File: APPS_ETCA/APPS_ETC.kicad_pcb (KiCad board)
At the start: 2 copper layers, 93.5 x 69.6 mm, 27 parts, among them P1 DTM1312PC12PDR008, U1 NUCLEO-L432KC, U2 MCP6004, U6 LM7805_TO220, U8 LM7809_TO220

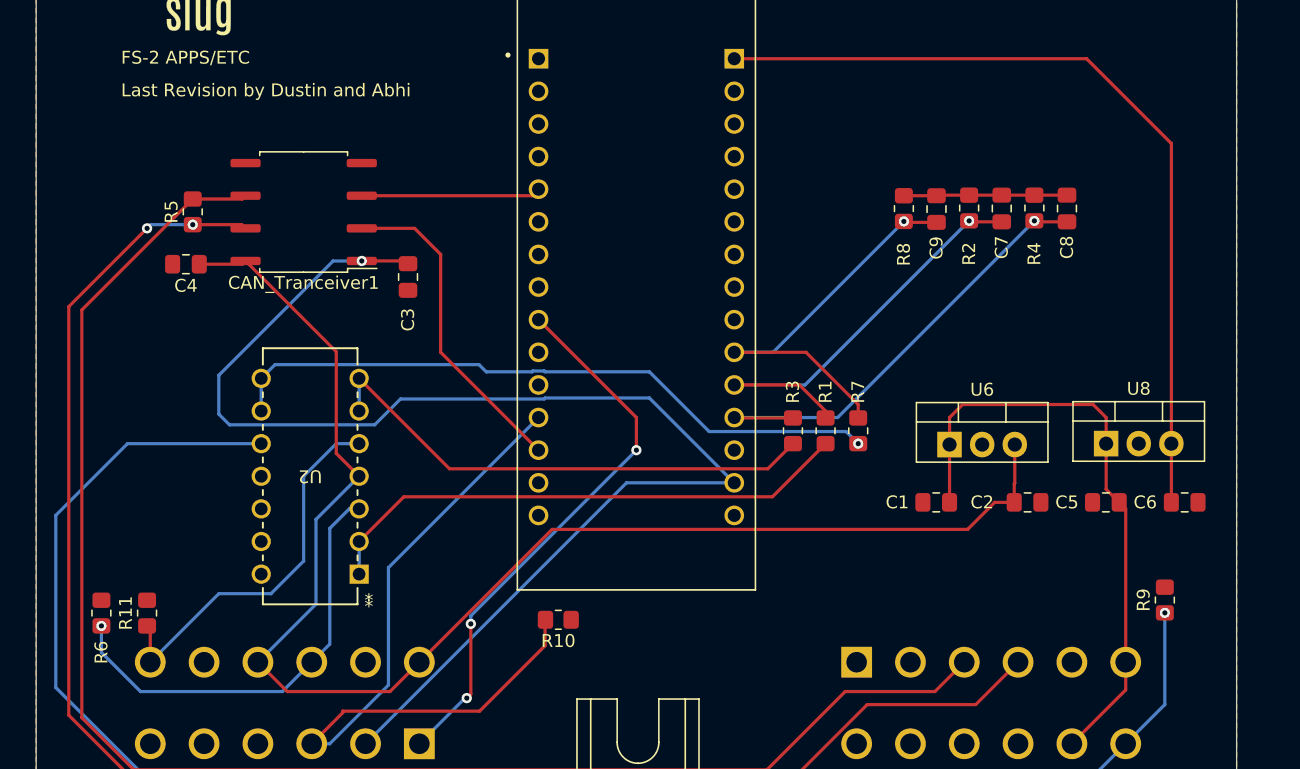
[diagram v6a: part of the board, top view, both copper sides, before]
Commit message: silk screen update again (please dont break)
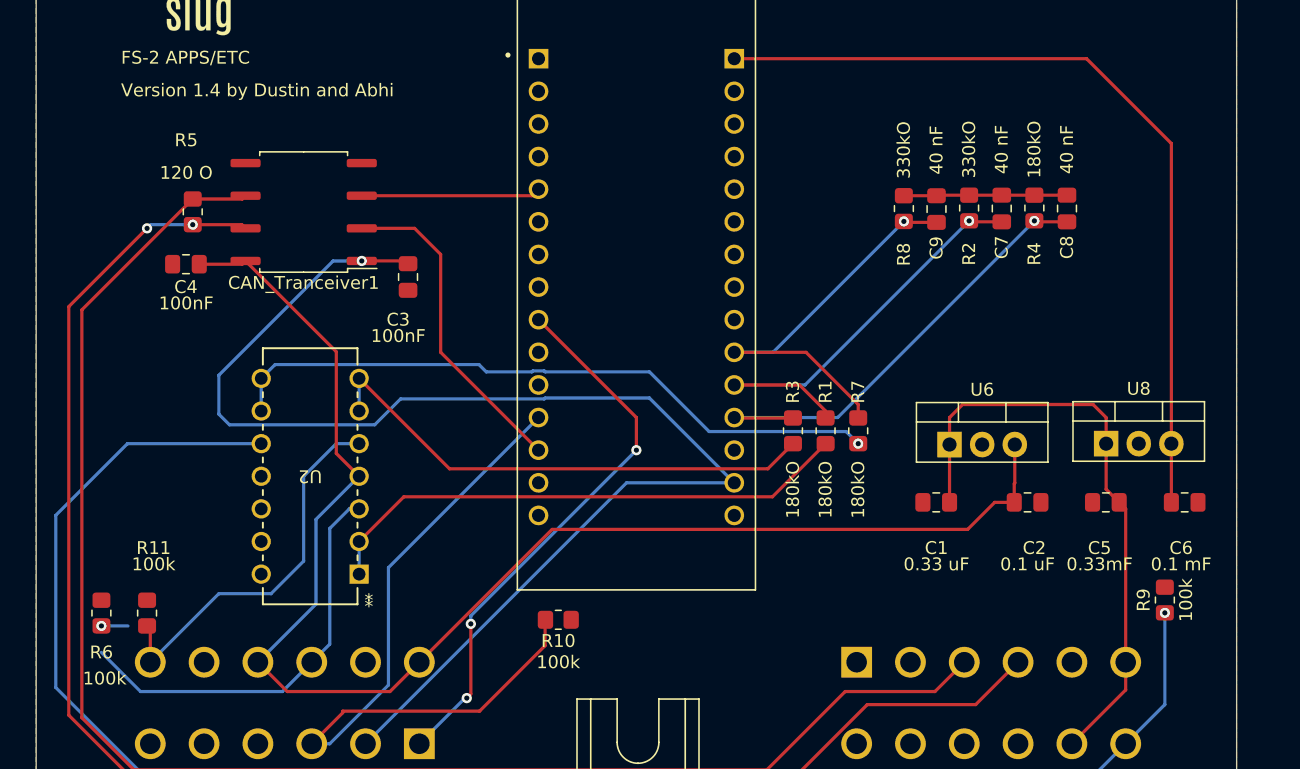
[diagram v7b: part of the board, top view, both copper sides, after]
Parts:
- C1: value 0.33 mF -> 0.33 uF
- C2: value 0.1 mF -> 0.1 uF
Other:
- board text added: "Version 1.4 by Dustin and Abhi"
- board text removed: "Last Revision by Dustin and Abhi"
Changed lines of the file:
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@@
         (effects (font (size 1 1) (thickness 0.15)))
     )
-    (fp_text value "100k" (at 0 1.65) (layer "F.Fab")
+    (fp_text value "100k" (at 0 -3.302) (layer "F.SilkS")
         (effects (font (size 1 1) (thickness 0.15)))
     )
@@
         (effects (font (size 1 1) (thickness 0.15)))
     )
-    (fp_text value "180kO" (at 4.556 0 90) (layer "F.Fab")
+    (fp_text value "180kO" (at 4.556 0 90) (layer "F.SilkS")
         (effects (font (size 1 1) (thickness 0.15)))
     )
@@
         (effects (font (size 1 1) (thickness 0.15)))
     )
-    (fp_text value "40 nF" (at 4.5935 0 90) (layer "F.Fab")
+    (fp_text value "40 nF" (at 4.5935 0 90) (layer "F.SilkS")
         (effects (font (size 1 1) (thickness 0.15)))
     )
@@
     (property "ki_keywords" "cap capacitor")
     (attr smd)
-    (fp_text reference "C4" (at 0 -1.68) (layer "F.SilkS")
+    (fp_text reference "C4" (at 0 -1.778) (layer "F.SilkS")
         (effects (font (size 1 1) (thickness 0.15)))
     )
-    (fp_text value "100nF" (at 0 1.68) (layer "F.Fab")
+    (fp_text value "100nF" (at -0.0215 -3.048) (layer "F.SilkS")
         (effects (font (size 1 1) (thickness 0.15)))
     )
@@
         (effects (font (size 1 1) (thickness 0.15)))
     )
-    (fp_text value "330kO" (at 4.556 0 90) (layer "F.Fab")
+    (fp_text value "330kO" (at 4.556 0 90) (layer "F.SilkS")
         (effects (font (size 1 1) (thickness 0.15)))
     )
@@
         (effects (font (size 1 1) (thickness 0.15)))
     )
-    (fp_text value "180kO" (at -4.588 0 90) (layer "F.Fab")
+    (fp_text value "180kO" (at -4.588 0 90) (layer "F.SilkS")
         (effects (font (size 1 1) (thickness 0.15)))
     )
@@
         (effects (font (size 1 1) (thickness 0.15)))
     )
-    (fp_text value "180kO" (at -4.588 0 90) (layer "F.Fab")
+    (fp_text value "180kO" (at -4.588 0 90) (layer "F.SilkS")
         (effects (font (size 1 1) (thickness 0.15)))
     )
@@
     (property "ki_keywords" "R res resistor")
     (attr smd)
-    (fp_text reference "R5" (at 0 -1.65 90) (layer "F.SilkS")
+    (fp_text reference "R5" (at 5.572 -0.508 180) (layer "F.SilkS")
         (effects (font (size 1 1) (thickness 0.15)))
     )
-    (fp_text value "120 O" (at 0 1.65 90) (layer "F.Fab")
+    (fp_text value "120 O" (at 3.032 -0.508 180) (layer "F.SilkS")
         (effects (font (size 1 1) (thickness 0.15)))
     )
@@
     (property "ki_keywords" "cap capacitor")
     (attr smd)
-    (fp_text reference "C5" (at 3.0265 0) (layer "F.SilkS")
+    (fp_text reference "C5" (at 0.4865 -3.556) (layer "F.SilkS")
         (effects (font (size 1 1) (thickness 0.15)))
     )
-    (fp_text value "0.33mF" (at 0 1.68) (layer "F.Fab")
+    (fp_text value "0.33mF" (at 0.4865 -4.826) (layer "F.SilkS")
         (effects (font (size 1 1) (thickness 0.15)))
     )
@@
     (property "ki_keywords" "cap capacitor")
     (attr smd)
-    (fp_text reference "C3" (at 3.3235 0 90) (layer "F.SilkS")
+    (fp_text reference "C3" (at 3.3235 0.762 -180) (layer "F.SilkS")
         (effects (font (size 1 1) (thickness 0.15)))
     )
-    (fp_text value "100nF" (at -0.2325 -2.032 90) (layer "F.Fab")
+    (fp_text value "100nF" (at 4.5935 0.762 -180) (layer "F.SilkS")
         (effects (font (size 1 1) (thickness 0.15)))
     )
@@
         (effects (font (size 1 1) (thickness 0.15)))
     )
-    (fp_text value "330kO" (at 4.556 0 90) (layer "F.Fab")
+    (fp_text value "330kO" (at 4.556 0 90) (layer "F.SilkS")
         (effects (font (size 1 1) (thickness 0.15)))
     )
@@
         (effects (font (size 1 1) (thickness 0.15)))
     )
-    (fp_text value "100k" (at 0 1.65 90) (layer "F.Fab")
+    (fp_text value "100k" (at 0 1.65 90) (layer "F.SilkS")
         (effects (font (size 1 1) (thickness 0.15)))
     )
@@
         (effects (font (size 1 1) (thickness 0.15)))
     )
-    (fp_text value "40 nF" (at 4.5935 0 90) (layer "F.Fab")
+    (fp_text value "40 nF" (at 4.5935 0 90) (layer "F.SilkS")
         (effects (font (size 1 1) (thickness 0.15)))
     )
@@
         (effects (font (size 1 1) (thickness 0.15)))
     )
-    (fp_text value "180kO" (at -4.588 0 90) (layer "F.Fab")
+    (fp_text value "180kO" (at -4.588 0 90) (layer "F.SilkS")
         (effects (font (size 1 1) (thickness 0.15)))
     )
@@
     (property "ki_keywords" "cap capacitor")
     (attr smd)
-    (fp_text reference "C1" (at 3.0265 0) (layer "F.SilkS")
+    (fp_text reference "C1" (at -0.0215 -3.556) (layer "F.SilkS")
         (effects (font (size 1 1) (thickness 0.15)))
     )
-    (fp_text value "0.33 mF" (at -0.0215 -2.032) (layer "F.Fab")
+    (fp_text value "0.33 uF" (at -0.0215 -4.826) (layer "F.SilkS")
         (effects (font (size 1 1) (thickness 0.15)))
     )
@@
     (property "ki_keywords" "cap capacitor")
     (attr smd)
-    (fp_text reference "C2" (at -3.5345 0) (layer "F.SilkS")
+    (fp_text reference "C2" (at 0.5295 3.556) (layer "F.SilkS")
         (effects (font (size 1 1) (thickness 0.15)))
     )
-    (fp_text value "0.1 mF" (at 0 1.68) (layer "F.Fab")
+    (fp_text value "0.1 uF" (at 0 4.826) (layer "F.SilkS")
         (effects (font (size 1 1) (thickness 0.15)))
     )
@@
         (effects (font (size 1 1) (thickness 0.15)))
     )
-    (fp_text value "40 nF" (at 4.5935 0 90) (layer "F.Fab")
+    (fp_text value "40 nF" (at 4.5935 0 90) (layer "F.SilkS")
         (effects (font (size 1 1) (thickness 0.15)))
     )
@@
     (property "ki_keywords" "R res resistor")
     (attr smd)
-    (fp_text reference "R6" (at -3.064 0 90) (layer "F.SilkS")
+    (fp_text reference "R6" (at -3.064 0 180) (layer "F.SilkS")
         (effects (font (size 1 1) (thickness 0.15)))
     )
-    (fp_text value "100k" (at 4.048 0 90) (layer "F.Fab")
+    (fp_text value "100k" (at -5.096 0.254 180) (layer "F.SilkS")
         (effects (font (size 1 1) (thickness 0.15)))
     )
@@
     (property "ki_keywords" "cap capacitor")
     (attr smd)
-    (fp_text reference "C6" (at -3.0695 0) (layer "F.SilkS")
+    (fp_text reference "C6" (at -0.2755 3.556) (layer "F.SilkS")
         (effects (font (size 1 1) (thickness 0.15)))
     )
-    (fp_text value "0.1 mF" (at 0 1.68) (layer "F.Fab")
+    (fp_text value "0.1 mF" (at -0.2755 4.826) (layer "F.SilkS")
         (effects (font (size 1 1) (thickness 0.15)))
     )
@@
     (property "ki_keywords" "R res resistor")
     (attr smd)
-    (fp_text reference "R11" (at 0 -1.65 90) (layer "F.SilkS")
+    (fp_text reference "R11" (at 5.064 0.508 180) (layer "F.SilkS")
         (effects (font (size 1 1) (thickness 0.15)))
     )
-    (fp_text value "100k" (at 0 1.65 90) (layer "F.Fab")
+    (fp_text value "100k" (at 3.794 0.508 180) (layer "F.SilkS")
         (effects (font (size 1 1) (thickness 0.15)))
     )
@@
     (effects (font (size 1 1) (thickness 0.15)) (justify left bottom))
   )
-  (gr_text "Last Revision by Dustin and Abhi" (at 142.24 79.248) (layer "F.SilkS")
+  (gr_text "Version 1.4 by Dustin and Abhi" (at 142.24 79.248) (layer "F.SilkS")
     (effects (font (size 1 1) (thickness 0.15)) (justify left bottom))
   )
@@
   (segment (start 154.806 125.476) (end 157.092 123.19) (width 0.25) (layer "B.Cu") (net 13))
   (segment (start 143.764 125.476) (end 154.806 125.476) (width 0.25) (layer "B.Cu") (net 13))
-  (segment (start 140.716 120.364) (end 140.716 122.428) (width 0.25) (layer "B.Cu") (net 13))
+  (segment (start 140.716 120.364) (end 142.78 120.364) (width 0.25) (layer "B.Cu") (net 13))
   (segment (start 158.496 121.786) (end 158.496 112.776) (width 0.25) (layer "B.Cu") (net 13))
   (via (at 223.52 119.348) (size 0.8) (drill 0.4) (layers "F.Cu" "B.Cu") (net 14))

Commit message: silkscreen final update
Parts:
- C5: value 0.33mF -> 0.33uF
- C6: value 0.1 mF -> 0.1 uF
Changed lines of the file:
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@@
     (property "ki_keywords" "cap capacitor")
     (attr smd)
-    (fp_text reference "C5" (at 0.4865 -3.556) (layer "F.SilkS")
-        (effects (font (size 1 1) (thickness 0.15)))
-    )
-    (fp_text value "0.33mF" (at 0.4865 -4.826) (layer "F.SilkS")
+    (fp_text reference "C5" (at 0.4865 -2.286) (layer "F.SilkS")
+        (effects (font (size 1 1) (thickness 0.15)))
+    )
+    (fp_text value "0.33uF" (at 0.4865 -3.556) (layer "F.SilkS")
         (effects (font (size 1 1) (thickness 0.15)))
     )
@@
     (property "ki_keywords" "cap capacitor")
     (attr smd)
-    (fp_text reference "C2" (at 0.5295 3.556) (layer "F.SilkS")
-        (effects (font (size 1 1) (thickness 0.15)))
-    )
-    (fp_text value "0.1 uF" (at 0 4.826) (layer "F.SilkS")
+    (fp_text reference "C2" (at -0.7405 2.286) (layer "F.SilkS")
+        (effects (font (size 1 1) (thickness 0.15)))
+    )
+    (fp_text value "0.1 uF" (at -0.7405 3.556) (layer "F.SilkS")
         (effects (font (size 1 1) (thickness 0.15)))
     )
@@
     (property "ki_keywords" "cap capacitor")
     (attr smd)
-    (fp_text reference "C6" (at -0.2755 3.556) (layer "F.SilkS")
-        (effects (font (size 1 1) (thickness 0.15)))
-    )
-    (fp_text value "0.1 mF" (at -0.2755 4.826) (layer "F.SilkS")
-        (effects (font (size 1 1) (thickness 0.15)))
-    )
+    (fp_text reference "C6" (at -0.2755 2.286) (layer "F.SilkS")
+        (effects (font (size 1 1) (thickness 0.15)))
+    )
+    (fp_text value "0.1 uF" (at -0.2755 3.556) (layer "F.SilkS")
+        (effects (font (size 1 1) (thickness 0.15)))
+    )
